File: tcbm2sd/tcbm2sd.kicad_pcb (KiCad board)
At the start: 2 copper layers, 56 x 91 mm, 13 parts, among them J2 JTAG, J3 debug, J4 AMS1117, J5 SD CARD, J7 debug, J8 C16-Exp-Port, U1 XC9572XL-VQ64, U2 Arduino_Pro_Mini

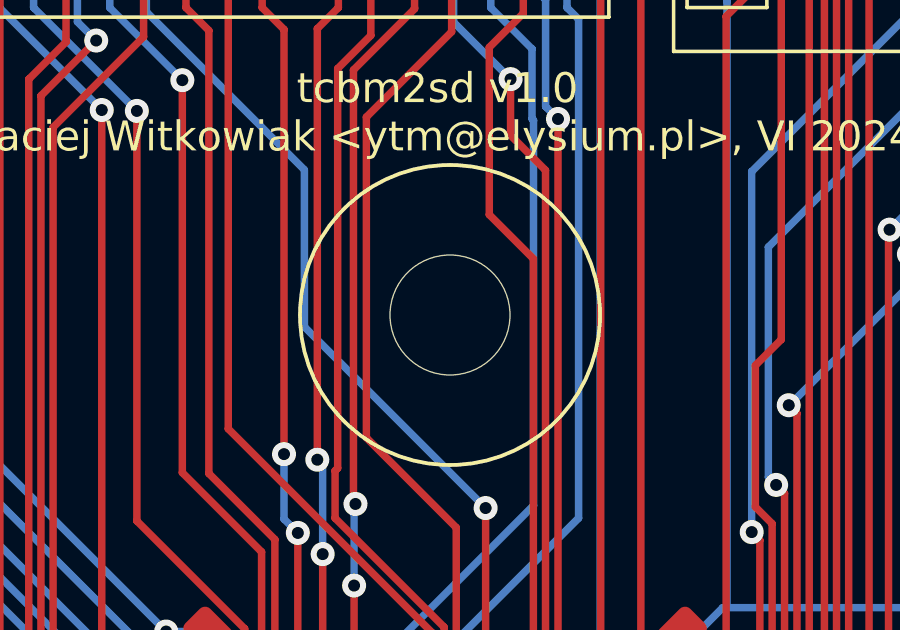
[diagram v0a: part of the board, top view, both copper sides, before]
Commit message: update comments, correct central hole size to 5mm
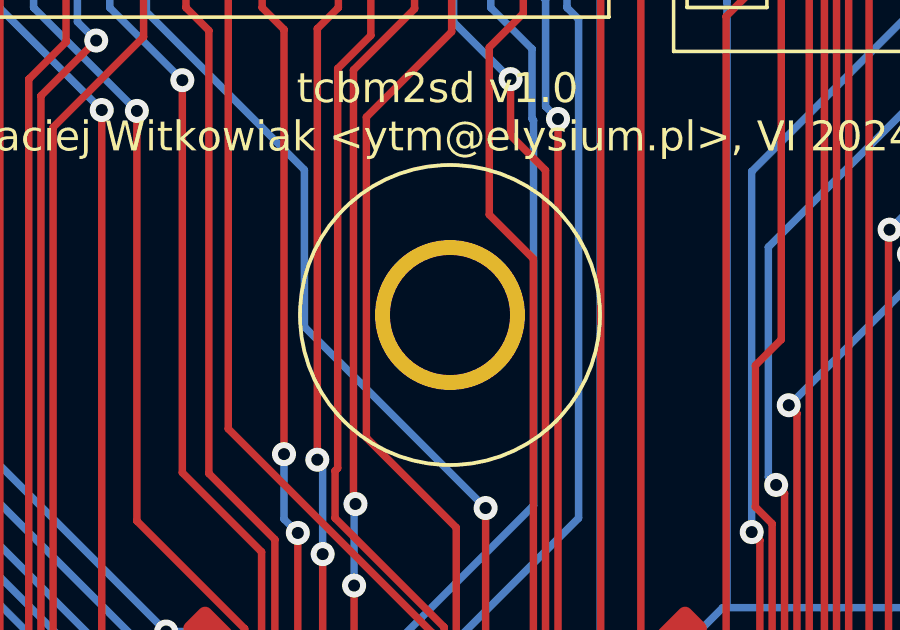
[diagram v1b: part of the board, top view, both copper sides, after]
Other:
- board text removed: "4mm"
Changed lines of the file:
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@@
     (fp_line (start 54 -10) (end 54 -91) (layer "Edge.Cuts") (width 0.05))
     (fp_line (start 1 0) (end 0 -1) (layer "Edge.Cuts") (width 0.05))
-    (pad "" np_thru_hole circle (at 26 -48.5) (size 4 4) (drill 4) (layers F&B.Cu *.Mask))
+    (pad "" np_thru_hole circle (at 26 -48.5) (size 5 5) (drill 4) (layers F&B.Cu *.Mask))
     (pad "1" smd roundrect (at 2 -5) (size 0.9 9.25) (layers "F.Cu" "F.Paste" "F.Mask") (roundrect_rratio 0.125)
       (net 17 "GND") (pinfunction "GND") (pintype "power_out") (solder_mask_margin 0.0508))
@@
     (effects (font (size 0.6 0.6) (thickness 0.15)))
   )
-  (gr_text "4mm" (at 148.336 104.648) (layer "Cmts.User")
-    (effects (font (size 1 1) (thickness 0.15)))
-  )
   (dimension (type aligned) (layer "Dwgs.User")

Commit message: clean pcb, new revision
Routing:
- net GND: track 261.3 -> 0.00 mm, vias 13 -> 0
- net +3V3: track 152.7 -> 0.00 mm, vias 7 -> 0
- net /A8: track 138.3 -> 0.00 mm, vias 4 -> 0
- net /A7: track 138.2 -> 0.00 mm, vias 3 -> 0
- net /A6: track 138.0 -> 0.00 mm, vias 3 -> 0
- net /A9: track 135.9 -> 0.00 mm, vias 3 -> 0
- net /A10: track 134.1 -> 0.00 mm, vias 5 -> 0
- net /A2: track 126.5 -> 0.00 mm, vias 4 -> 0
- net /A3: track 125.1 -> 0.00 mm, vias 3 -> 0
- net /A4: track 123.7 -> 0.00 mm, vias 4 -> 0
- net /A5: track 120.3 -> 0.00 mm, vias 5 -> 0
- net /A1: track 118.9 -> 0.00 mm, vias 3 -> 0
- net /A13: track 117.2 -> 0.00 mm, vias 3 -> 0
- net /A0: track 116.9 -> 0.00 mm, vias 3 -> 0
- net /PHI0: track 115.3 -> 0.00 mm, vias 2 -> 0
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
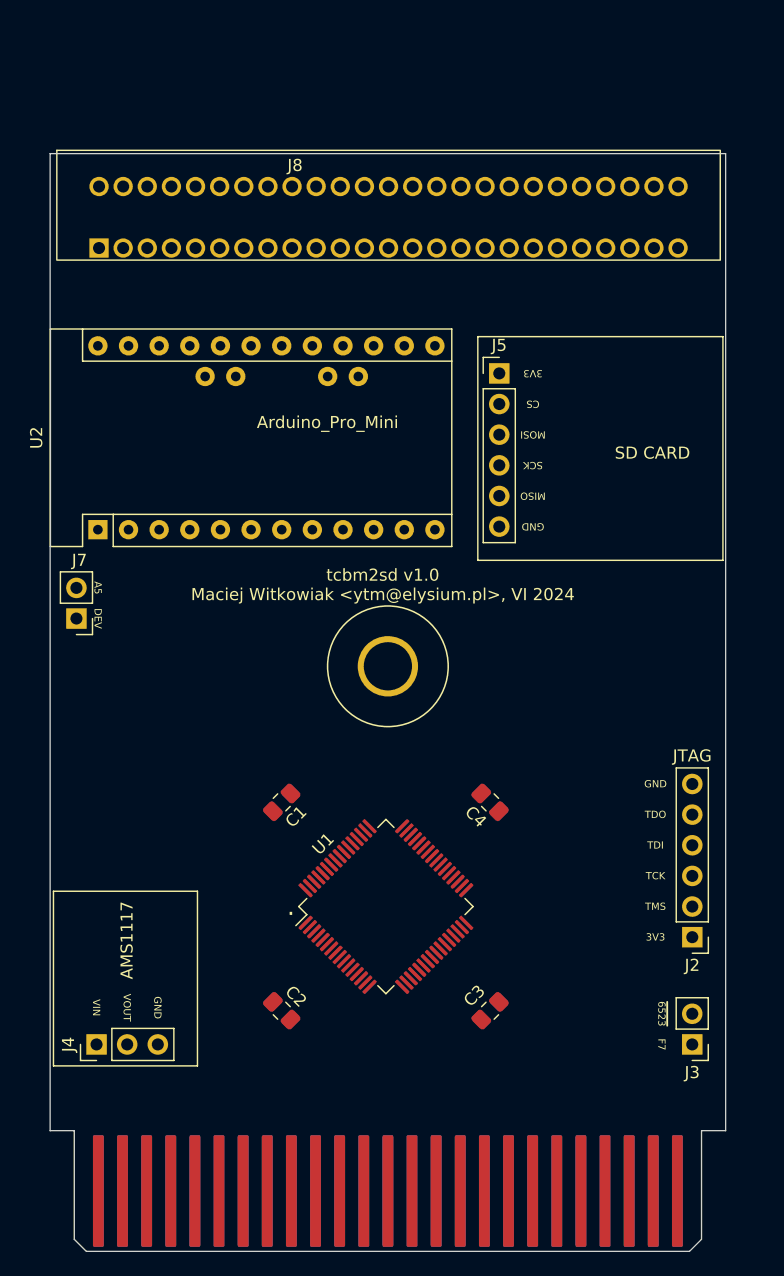
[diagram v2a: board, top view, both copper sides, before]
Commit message: - solder jumpers to choose DEV from +33V/GND/A4/D1 - TCBM connector - removed debug pads - RESET 3.3V, through solder jumper - cut connection to Arduino pin 3 (RP2040 clone has GND there) - VCC net class with wider trace
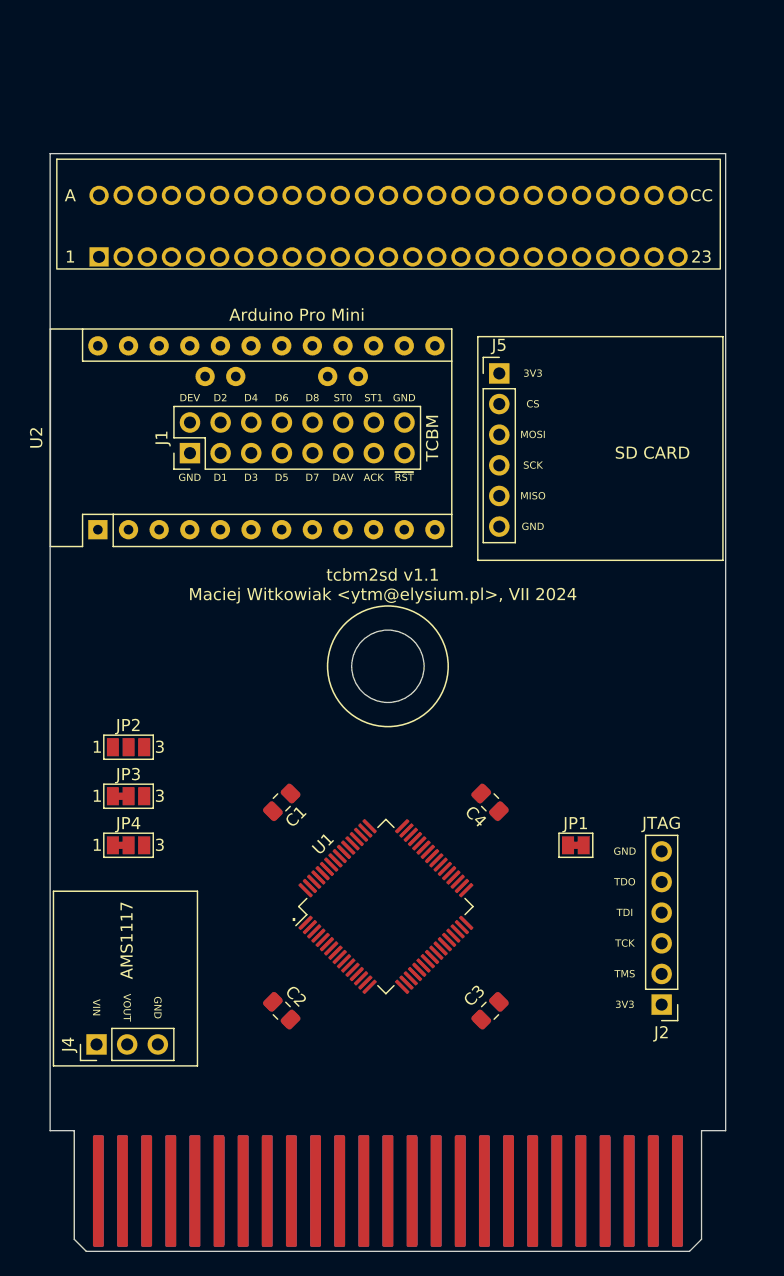
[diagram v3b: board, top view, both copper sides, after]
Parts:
- removed J3, J7: debug, Connector_PinHeader_2.54mm:PinHeader_1x02_P2.54mm_Vertical
- added J1: TCBM, Connector_PinHeader_2.54mm:PinHeader_2x08_P2.54mm_Vertical, F.Cu at (132.1, 84.3)
- added JP1: SolderJumper_2_Bridged, Jumper:SolderJumper-2_P1.3mm_Bridged_Pad1.0x1.5mm, F.Cu at (164.1, 116.8)
- added JP2: SolderJumper_3_Open, Jumper:SolderJumper-3_P1.3mm_Open_Pad1.0x1.5mm_NumberLabels, F.Cu at (127.0, 108.7)
- added JP3: SolderJumper_3_Bridged12, Jumper:SolderJumper-3_P1.3mm_Bridged12_Pad1.0x1.5mm_NumberLabels, F.Cu at (127.0, 112.8)
- added JP4: SolderJumper_3_Bridged12, Jumper:SolderJumper-3_P1.3mm_Bridged12_Pad1.0x1.5mm_NumberLabels, F.Cu at (127.0, 116.8)
- U2: value Arduino_Pro_Mini -> Arduino Pro Mini
- moved J2 6.14 mm to (171.2, 130.0)
- moved J8 0.74 mm to (130.6, 63.0)
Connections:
- U1 pad 44: unconnected-(U1-Pad44) -> /~{RESET_3_3V}
- U2 pad 2: unconnected-(U2-Pad2) -> Net-(U2-Pad2)
- U2 pad 22: /~{RESET} -> Net-(U2-Pad22)
- U2 pad 3: /~{RESET} -> unconnected-(U2-Pad3)
- U2 pad A4: /DEV -> Net-(U2-PadA4)
- U2 pad A5: Net-(J7-Pad2) -> unconnected-(U2-PadA5)
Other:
- board text added: "1"
- board text added: "23"
- board text added: "A"
- board text added: "ACK"
- board text added: "CC"
- board text added: "D1"
- board text added: "D2"
- board text added: "D3"
- board text added: "D4"
- board text added: "D5"
- board text added: "D6"
- board text added: "D7"
- board text added: "D8"
- board text added: "DAV"
- board text added: "JP1: pass computer reset to Arduino JP2: select h/w DEV #9 (1-2) or #8 (2-3) JP3: select s/w DEV from A4 (1-2) or D1 (2-3) JP4: select s/w DEV (1-2) or h/w DEV (2-3)"
- board text added: "ST0"
- board text added: "ST1"
- board text added: "https://github.com/ytmytm/plus4-tcbm2sd"
- board text added: "tcbm2sd v1.1 Maciej Witkowiak <ytm@elysium.pl>, VII 2024"
- board text added: "~{RST}"
- board text removed: "A5"
- board text removed: "F7"
- board text removed: "tcbm2sd v1.0 Maciej Witkowiak <ytm@elysium.pl>, VI 2024"
- board text removed: "~{6523}"

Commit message: freerouter results (with hole set to 6mm), now back to 5mm
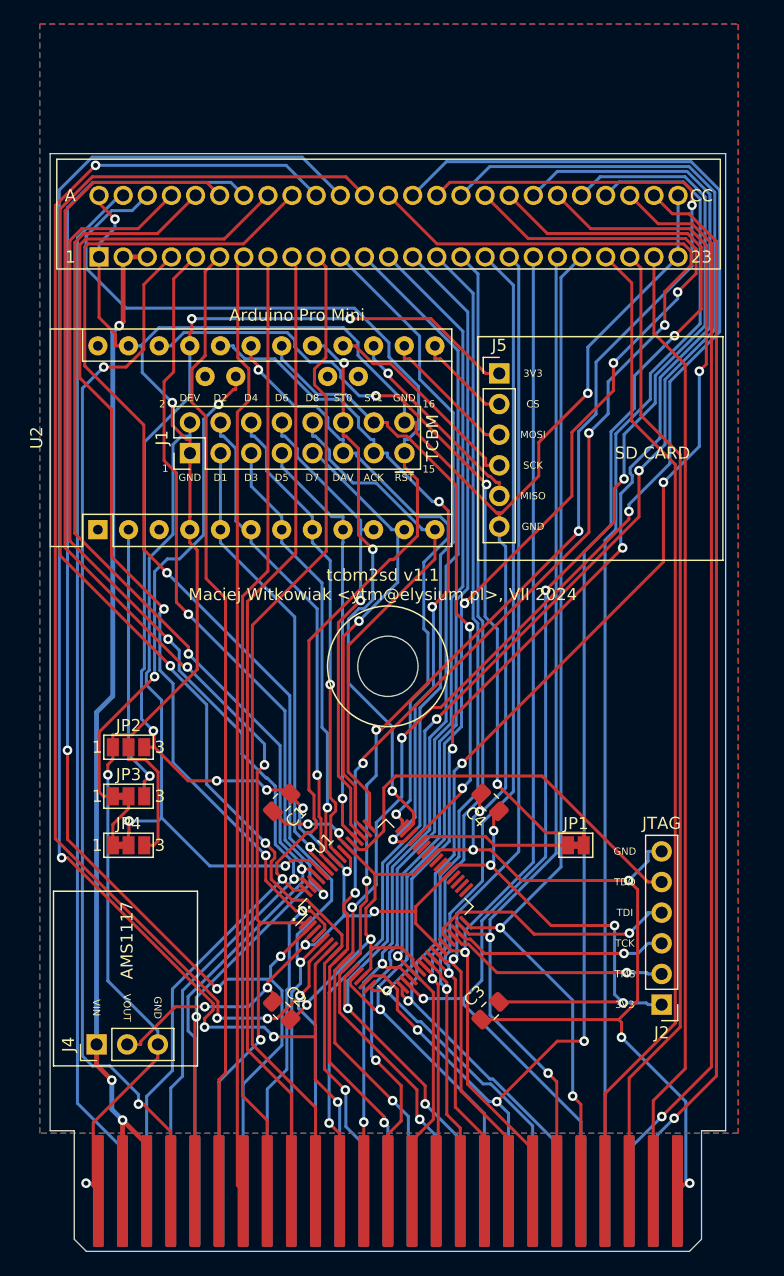
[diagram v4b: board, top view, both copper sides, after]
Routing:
- net GND: track 0.00 -> 303.5 mm, vias 0 -> 14
- net +3V3: track 0.00 -> 173.7 mm, vias 0 -> 15
- net /A10: track 0.00 -> 132.0 mm, vias 0 -> 4
- net /A11: track 0.00 -> 126.7 mm, vias 0 -> 4
- net /A7: track 0.00 -> 126.5 mm, vias 0 -> 4
- net /~{RESET}: track 0.00 -> 122.1 mm, vias 0 -> 1
- net /A5: track 0.00 -> 121.4 mm, vias 0 -> 4
- net /A3: track 0.00 -> 121.1 mm, vias 0 -> 4
- net /A6: track 0.00 -> 120.5 mm, vias 0 -> 5
- net /A8: track 0.00 -> 119.6 mm, vias 0 -> 5
- net /A2: track 0.00 -> 117.4 mm, vias 0 -> 3
- net /A9: track 0.00 -> 117.1 mm, vias 0 -> 3
- net /A4: track 0.00 -> 116.5 mm, vias 0 -> 4
- net /A14: track 0.00 -> 115.5 mm, vias 0 -> 3
- net /A0: track 0.00 -> 111.6 mm, vias 0 -> 3
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- added copper zone on B.Cu, net GND
- added copper zone on F.Cu, net GND
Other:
- board text added: "15"
- board text added: "16"
- board text added: "2"
- board text added: "JP1: pass computer reset to Arduino JP2: select h/w DEV #9 (1-2) or #8 (2-3) JP3: select s/w DEV from A4 (1-2) or RX (D0) (2-3) JP4: select s/w DEV (1-2) or h/w DEV (2-3)"
- board text removed: "JP1: pass computer reset to Arduino JP2: select h/w DEV #9 (1-2) or #8 (2-3) JP3: select s/w DEV from A4 (1-2) or D1 (2-3) JP4: select s/w DEV (1-2) or h/w DEV (2-3)"

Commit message: drop PLA outputs, use more exp. port inputs to CPLD (just in case) own SMD 3.3V regulator circuit own SD card circuit (SD card model etc.) from SD2IEC plug https://www.hackup.net/2018/10/sd2iecplug-v2-0/
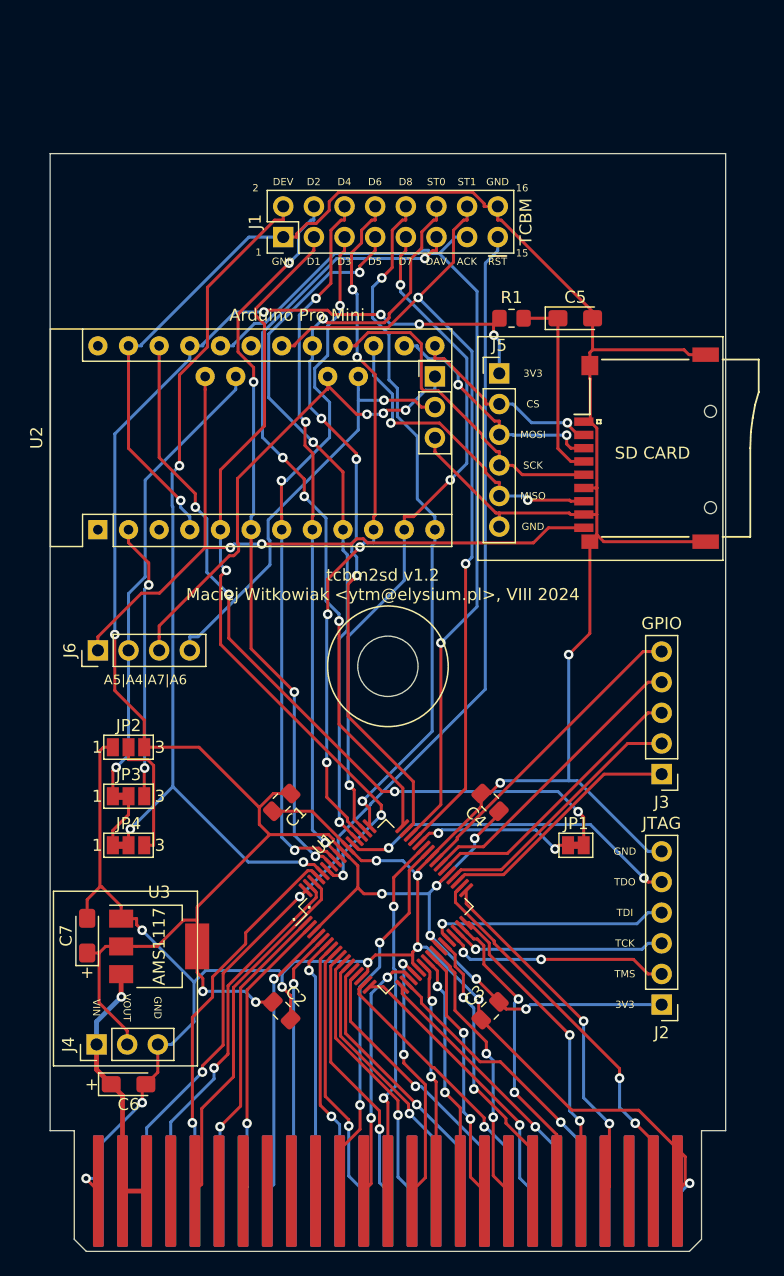
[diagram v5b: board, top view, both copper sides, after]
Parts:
- removed J8: C16-Exp-Port, LittleSixteen:50Pin_Edge_Connector_C16
- added C5: 10µ, Capacitor_Tantalum_SMD:CP_EIA-3216-12_Kemet-S_Pad1.58x1.35mm_HandSolder, F.Cu at (164.0, 73.2)
- added C6: 10µ, Capacitor_Tantalum_SMD:CP_EIA-3216-12_Kemet-S_Pad1.58x1.35mm_HandSolder, F.Cu at (127.0, 136.7)
- added C7: 10µ, Capacitor_Tantalum_SMD:CP_EIA-3216-12_Kemet-S_Pad1.58x1.35mm_HandSolder, F.Cu at (123.6, 124.3)
- added J3: GPIO, Connector_PinHeader_2.54mm:PinHeader_1x05_P2.54mm_Vertical, F.Cu at (171.2, 110.9)
- added J6: ALT_A4_A7, Connector_PinHeader_2.54mm:PinHeader_1x04_P2.54mm_Vertical, F.Cu at (124.5, 100.7)
- added J7: ALT_A6_A7, Connector_PinHeader_2.54mm:PinHeader_1x03_P2.54mm_Vertical, F.Cu at (152.4, 78.0)
- added R1: 2.2R, Resistor_SMD:R_0805_2012Metric_Pad1.20x1.40mm_HandSolder, F.Cu at (158.8, 73.2)
- added U3: AMS1117-3.3, Package_TO_SOT_SMD:SOT-223-3_TabPin2, F.Cu at (129.5, 125.2)
- added XS1: SD connector, SD2IECplug:Conn_uSDcard, F.Cu at (175.2, 83.9)
- moved J1 19.5 mm to (139.8, 66.4)
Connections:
- net Net-(U2-PadA4) renamed /ALT_A4
- U1 pad 33: /F7 -> /AEC
- U1 pad 34: /~{6523_F0} -> /PHI2
- U1 pad 35: unconnected-(U1-Pad35) -> Net-(J3-Pad1)
- U1 pad 36: unconnected-(U1-Pad36) -> Net-(J3-Pad2)
- U1 pad 38: unconnected-(U1-Pad38) -> Net-(J3-Pad3)
- U1 pad 39: unconnected-(U1-Pad39) -> Net-(J3-Pad4)
- U1 pad 40: unconnected-(U1-Pad40) -> Net-(J3-Pad5)
- U1 pad 42: unconnected-(U1-Pad42) -> /~{CAS}
- U1 pad 43: unconnected-(U1-Pad43) -> /BA
- U2 pad A5: unconnected-(U2-PadA5) -> /SD_CD
- U2 pad A6: unconnected-(U2-PadA6) -> /ALT_A6
- U2 pad A7: unconnected-(U2-PadA7) -> /ALT_A7
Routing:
- net /A10: track 132.0 -> 21.2 mm, vias 4 -> 1
- net /A11: track 126.7 -> 21.3 mm, vias 4 -> 1
- net /A7: track 126.5 -> 22.0 mm, vias 4 -> 1
- net /A5: track 121.4 -> 22.5 mm, vias 4 -> 1
- net /A3: track 121.1 -> 22.8 mm, vias 4 -> 1
- net /A6: track 120.5 -> 22.2 mm, vias 5 -> 1
- net /A8: track 119.6 -> 21.7 mm, vias 5 -> 1
- net /A9: track 117.1 -> 21.4 mm, vias 3 -> 1
- net /NC1: track 94.4 -> 0.00 mm
- net /A2: track 117.4 -> 23.2 mm, vias 3 -> 1
- net /A4: track 116.5 -> 23.1 mm, vias 4 -> 1
- net /A14: track 115.5 -> 24.2 mm, vias 3 -> 1
- net /A12: track 109.9 -> 21.9 mm, vias 2 -> 1
- net /A0: track 111.6 -> 24.3 mm, vias 3 -> 1
- net /NC2: track 86.3 -> 0.00 mm, vias 1 -> 0
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- removed copper zone on B.Cu, net GND
- removed copper zone on F.Cu, net GND
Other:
- board text added: "+"
- board text added: "A5|A4|A7|A6"
- board text added: "tcbm2sd v1.2 Maciej Witkowiak <ytm@elysium.pl>, VIII 2024"
- board text removed: "23"
- board text removed: "A"
- board text removed: "CC"
- board text removed: "tcbm2sd v1.1 Maciej Witkowiak <ytm@elysium.pl>, VII 2024"
